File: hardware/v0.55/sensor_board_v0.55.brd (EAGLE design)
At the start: 56.4 x 41.9 mm, 59 parts, among them J3 USB-MICROB, J6 AVR_SPI_PRG_6PTH, U1 ATMEGA328P, U10 TSL2591, U11 915MHz, U2 SHT35, U3 OPA344, U5 FT231XS, U6 ADMP401, U7 PMS7003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

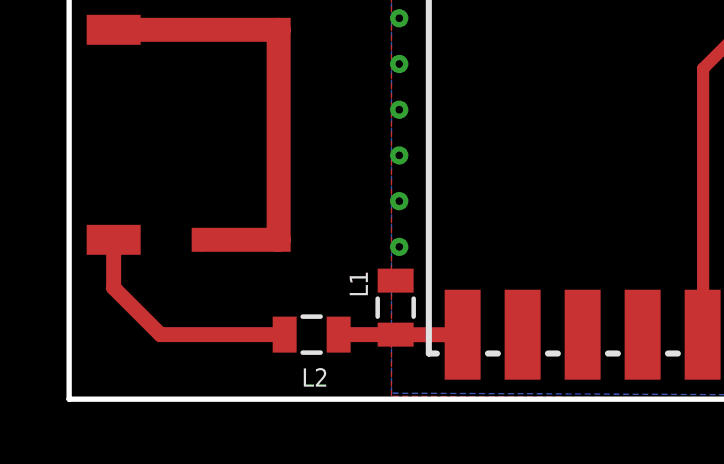
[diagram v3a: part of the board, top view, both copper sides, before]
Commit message: Added trace for wire monopole antenna
- wire antenna can be used by means of a jumper (in the event that chip
antenna doesn't work - make sure to desolder the chip antenna +
components)
- not sure of performance of chip + wire antenna trace (with
disconnected jumper) - maybe the trace adds capacitance or random noise?
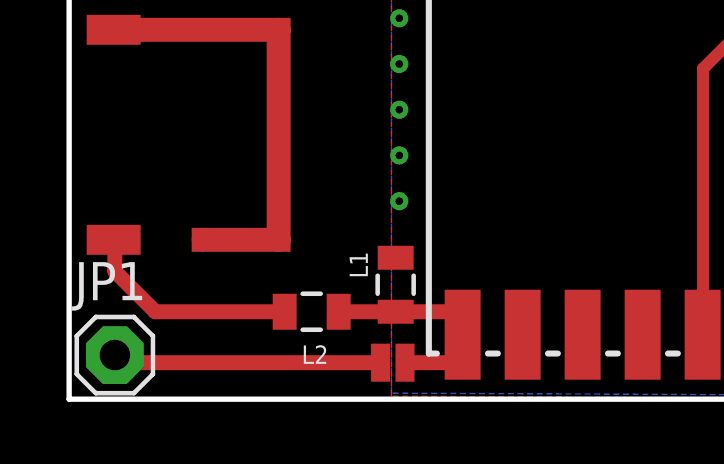
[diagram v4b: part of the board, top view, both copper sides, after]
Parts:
- added JP1: (no value), adafruit:1X01
- added JP3: JUMPER-PAD-2-NC_BY_PASTENO-SILK, SparkFun-Passives:PAD-JUMPER-2-NC_BY_PASTE_NO_SILK
- moved L1 0.76 mm to (11.9, 9.20)
- moved L2 0.76 mm to (9.10, 8.30)
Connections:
- new net N$6: JP1.1, JP3.2
- net FEED: now also JP3.1
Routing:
- net N$6: track 0.00 -> 8.96 mm
- net FEED: track 4.13 -> 7.76 mm
- net N$1: track 7.95 -> 7.28 mm
- net GND: vias 49 -> 48

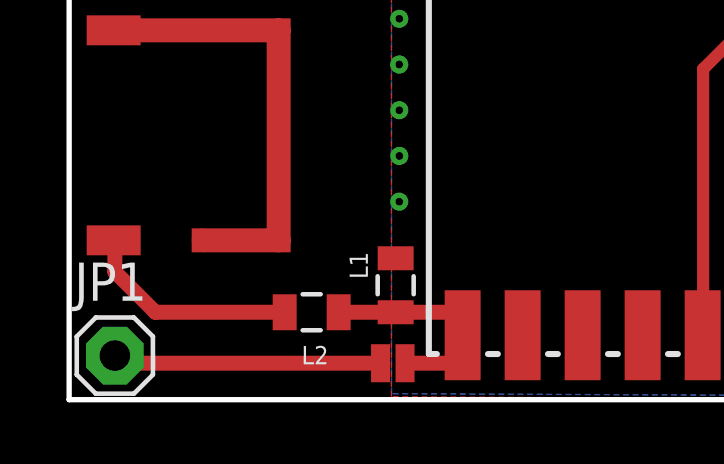
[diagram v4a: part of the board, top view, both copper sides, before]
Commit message: Redesigned antenna trace
- Removed trace for wire monopole (it needs GND plane underneath, so
wouldn't have worked anyway)
- Added jumper for SMD feed (if chip doesn't work, remove jumper, solder
wire monopole directly to radio ANT pad
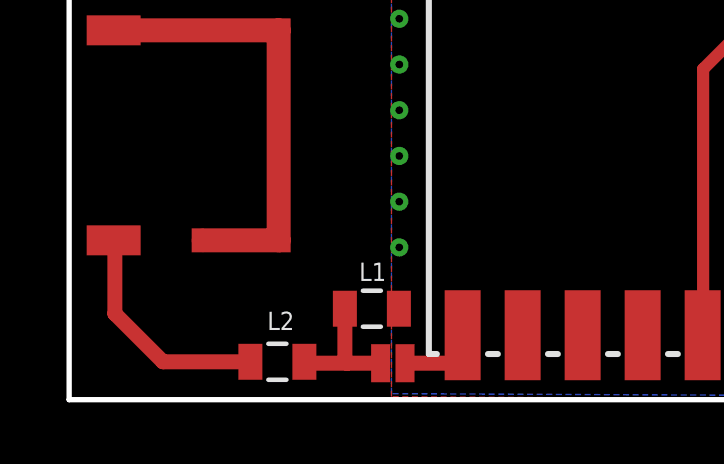
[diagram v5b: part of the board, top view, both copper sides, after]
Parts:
- removed JP1: (no value), adafruit:1X01
- moved L2 2.01 mm to (7.96, 6.65)
- moved L1 1.11 mm to (11.1, 8.42), turned to 0 degrees
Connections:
- net FEED: now also JP3.2; no longer JP3.1, U11.9
- net N$6: now also JP3.1, U11.9; no longer JP1.1, JP3.2
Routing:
- net N$6: track 8.96 -> 2.85 mm
- net FEED: track 7.76 -> 4.44 mm
- net GND: vias 48 -> 49
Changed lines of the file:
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@@
 </element>
 <element name="U$4" library="johanson-technology" package="SMD_CHIP" value="0868AT43A0020E" x="2.5" y="10.7" rot="R90"/>
-<element name="L1" library="SparkFun-Passives" package="0805" value="12nH" x="11.9" y="9.202" smashed="yes" rot="R90">
-<attribute name="NAME" x="10.9745" y="9.413" size="0.6096" layer="121" font="vector" rot="R90"/>
-<attribute name="PROD_ID" value="NDUC-13076" x="11.9" y="9.202" size="1.778" layer="27" rot="R90" display="off"/>
+<element name="L1" library="SparkFun-Passives" package="0805" value="12nH" x="11.107" y="8.42" smashed="yes">
+<attribute name="NAME" x="10.683" y="9.3455" size="0.6096" layer="121" font="vector"/>
+<attribute name="PROD_ID" value="NDUC-13076" x="11.107" y="8.42" size="1.778" layer="27" display="off"/>
 </element>
-<element name="L2" library="SparkFun-Passives" package="0805" value="1.8nH" x="9.1" y="8.302" smashed="yes" rot="R180">
-<attribute name="NAME" x="9.662" y="7.1765" size="0.6096" layer="121" font="vector" rot="R180"/>
-<attribute name="PROD_ID" value="NDUC-13076" x="9.1" y="8.302" size="1.778" layer="27" rot="R180" display="off"/>
+<element name="L2" library="SparkFun-Passives" package="0805" value="1.8nH" x="7.957" y="6.651" smashed="yes" rot="R180">
+<attribute name="NAME" x="8.519" y="8.3195" size="0.6096" layer="121" font="vector" rot="R180"/>
+<attribute name="PROD_ID" value="NDUC-13076" x="7.957" y="6.651" size="1.778" layer="27" rot="R180" display="off"/>
 </element>
-<element name="JP1" library="adafruit" package="1X01" value="" x="2.54" y="6.858"/>
-<element name="JP3" library="SparkFun-Passives" package="PAD-JUMPER-2-NC_BY_PASTE_NO_SILK" value="JUMPER-PAD-2-NC_BY_PASTENO-SILK" x="11.811" y="6.604" smashed="yes" rot="R180">
-<attribute name="VALUE" x="12.7635" y="8.255" size="0.4064" layer="27" rot="R180"/>
-</element>
+<element name="JP3" library="SparkFun-Passives" package="PAD-JUMPER-2-NC_BY_PASTE_NO_SILK" value="JUMPER-PAD-2-NC_BY_PASTENO-SILK" x="11.811" y="6.604" smashed="yes" rot="R180"/>
 </elements>
 <signals>
@@
 <via x="25.0864" y="19.9248" extent="1-16" drill="0.254" diameter="0.127"/>
 <contactref element="L1" pad="2"/>
-<wire x1="26.0096" y1="31.9848" x2="26.0096" y2="30.3848" width="0" layer="19" extent="1-1"/>
+<via x="12.0208" y="10.4648" extent="1-16" drill="0.254" diameter="0.127"/>
+<wire x1="26.0096" y1="30.3848" x2="26.0096" y2="31.9848" width="0" layer="19" extent="1-1"/>
 </signal>
 <signal name="VCC">
@@
 </signal>
 <signal name="FEED">
-<contactref element="U11" pad="9"/>
 <contactref element="L2" pad="1"/>
 <contactref element="L1" pad="1"/>
-<wire x1="14.05" y1="8.302" x2="11.9" y2="8.302" width="0.5" layer="1"/>
-<wire x1="14.05" y1="8.302" x2="14.097" y2="8.255" width="0.5" layer="1"/>
-<wire x1="14.097" y1="8.255" x2="14.097" y2="7.5726" width="0.5" layer="1"/>
-<wire x1="14.1328" y1="7.5368" x2="14.097" y2="7.5726" width="0.5" layer="1"/>
-<wire x1="11.9" y1="8.302" x2="10" y2="8.302" width="0.5" layer="1"/>
-<contactref element="JP3" pad="1"/>
-<wire x1="12.2119" y1="6.604" x2="14.097" y2="6.604" width="0.5" layer="1"/>
-<wire x1="14.097" y1="6.604" x2="14.224" y2="6.731" width="0.5" layer="1"/>
-<wire x1="14.224" y1="6.731" x2="14.224" y2="7.4456" width="0.5" layer="1"/>
-<wire x1="14.224" y1="7.4456" x2="14.1328" y2="7.5368" width="0.5" layer="1"/>
+<contactref element="JP3" pad="2"/>
+<wire x1="10.287" y1="6.604" x2="11.3983" y2="6.604" width="0.5" layer="1"/>
+<wire x1="10.287" y1="6.604" x2="8.857" y2="6.604" width="0.5" layer="1"/>
+<wire x1="8.857" y1="6.604" x2="8.857" y2="6.651" width="0.5" layer="1"/>
+<wire x1="10.207" y1="8.42" x2="10.207" y2="6.684" width="0.5" layer="1"/>
+<wire x1="10.207" y1="6.684" x2="10.287" y2="6.604" width="0.5" layer="1"/>
 </signal>
 <signal name="N$7">
@@
 <contactref element="L2" pad="2"/>
 <contactref element="U$4" pad="P$1"/>
-<wire x1="2.54" y1="9.652" x2="2.54" y2="10.66" width="0.5" layer="1"/>
 <wire x1="2.54" y1="10.66" x2="2.5" y2="10.7" width="0.5" layer="1"/>
-<wire x1="8.2" y1="8.302" x2="3.89" y2="8.302" width="0.5" layer="1"/>
-<wire x1="3.89" y1="8.302" x2="2.54" y2="9.652" width="0.5" layer="1"/>
+<wire x1="7.057" y1="6.651" x2="4.144" y2="6.651" width="0.5" layer="1"/>
+<wire x1="4.144" y1="6.651" x2="2.54" y2="8.255" width="0.5" layer="1"/>
+<wire x1="2.54" y1="8.255" x2="2.54" y2="10.66" width="0.5" layer="1"/>
 </signal>
 <signal name="N$6">
-<contactref element="JP1" pad="1"/>
-<contactref element="JP3" pad="2"/>
-<wire x1="11.3983" y1="6.604" x2="2.794" y2="6.604" width="0.5" layer="1"/>
-<wire x1="2.794" y1="6.604" x2="2.54" y2="6.858" width="0.5" layer="1"/>
+<contactref element="U11" pad="9"/>
+<contactref element="JP3" pad="1"/>
+<wire x1="12.2119" y1="6.604" x2="14.1328" y2="6.604" width="0.5" layer="1"/>
+<wire x1="14.1328" y1="6.604" x2="14.1328" y2="7.5368" width="0.5" layer="1"/>
 </signal>
 </signals>
